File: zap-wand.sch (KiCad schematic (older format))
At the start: 15 parts, among them IC1 NC7WZ02, Q1 Q_PMOS_GDS, SW1 SW_PUSH_SMALL, U1 NCP4683DSQ33T1G

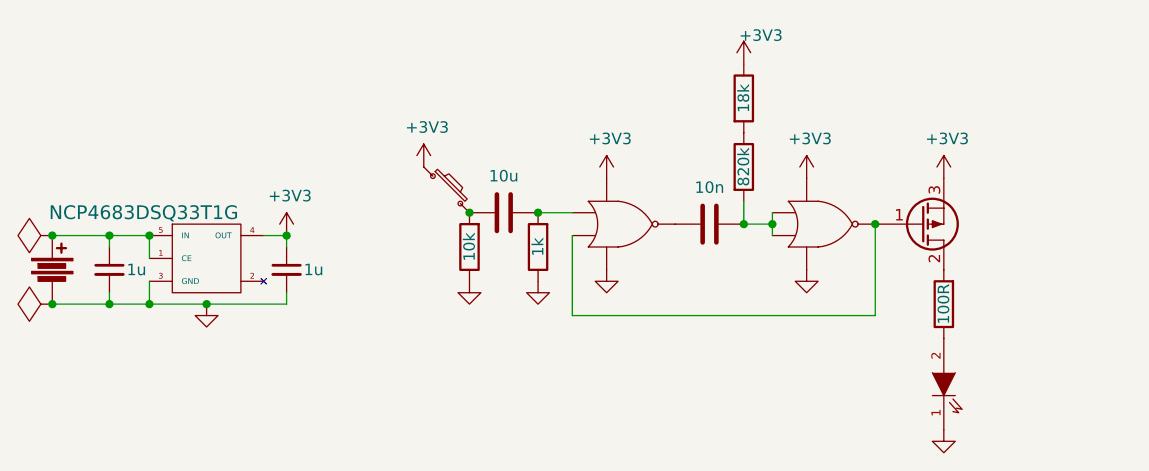
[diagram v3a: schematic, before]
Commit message: Added xor output inverter
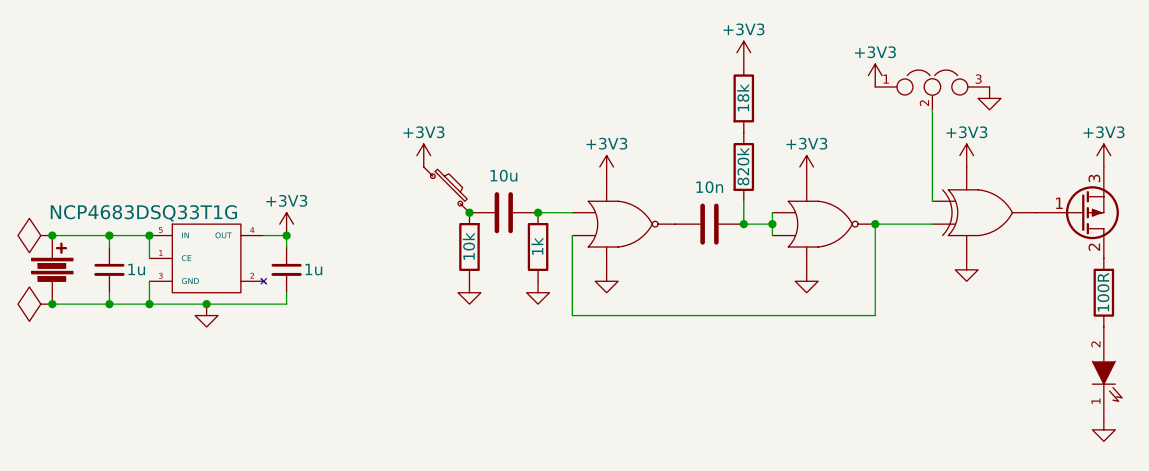
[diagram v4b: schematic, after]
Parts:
- added IC2: NC7SZ86, agg:SC-70-5, symbol NC7SZ86
- added JP1: JUMPER3, parts:solder_jumper_3, symbol JUMPER3
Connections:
- net +3V3: now also IC2.5 (VCC), JP1.1
- net GND: now also IC2.3 (GND), JP1.3
- net at IC1.2 (B1), IC1.3 (Y2): now also IC2.2 (B); no longer Q1.1 (G)
- new net: IC2.4 (Y), Q1.1 (G)
- new net: IC2.1 (A), JP1.2
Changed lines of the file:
@@
 LIBS:ncp103
 LIBS:ncp4683dsqxxt1g
+LIBS:nc7sz86
 LIBS:zap-wand-cache
 EELAYER 25 0
@@
 L LED D1
 U 1 1 578BAA6D
-P 5050 2550
-F 0 "D1" H 5096 2442 50  0001 R CNN
-F 1 "LED" V 5050 2442 50  0001 R CNN
-F 2 "agg:SIL-254P-02" H 5050 2550 50  0001 C CNN
-F 3 "" H 5050 2550 50  0000 C CNN
-	1    5050 2550
+P 5750 2500
+F 0 "D1" H 5796 2392 50  0001 R CNN
+F 1 "LED" V 5750 2392 50  0001 R CNN
+F 2 "agg:SIL-254P-02" H 5750 2500 50  0001 C CNN
+F 3 "" H 5750 2500 50  0000 C CNN
+	1    5750 2500
 	0    -1   -1   0
 $EndComp
@@
 L R R3
 U 1 1 578BAE5F
-P 5050 2200
-F 0 "R3" H 4980 2154 50  0001 R CNN
-F 1 "100R" V 5050 2200 50  0000 C CNN
-F 2 "agg:0603" V 4980 2200 50  0001 C CNN
-F 3 "http://www.farnell.com/datasheets/1849611.pdf?_ga=1.214886046.860814275.1465901405" H 5050 2200 50  0001 C CNN
-F 4 "2447227" H 5050 2200 60  0001 C CNN "Farnell"
-	1    5050 2200
+P 5750 2150
+F 0 "R3" H 5680 2104 50  0001 R CNN
+F 1 "100R" V 5750 2150 50  0000 C CNN
+F 2 "agg:0603" V 5680 2150 50  0001 C CNN
+F 3 "http://www.farnell.com/datasheets/1849611.pdf?_ga=1.214886046.860814275.1465901405" H 5750 2150 50  0001 C CNN
+F 4 "2447227" H 5750 2150 60  0001 C CNN "Farnell"
+	1    5750 2150
 	-1   0    0    1
 $EndComp
@@
 L Q_PMOS_GDS Q1
 U 1 1 578BD32A
-P 4950 1850
-F 0 "Q1" H 5141 1850 50  0001 L CNN
-F 1 "Q_PMOS_GDS" H 5141 1805 50  0001 L CNN
-F 2 "agg:SOT-323" H 5150 1950 50  0001 C CNN
-F 3 "http://www.farnell.com/datasheets/1508398.pdf?_ga=1.16462774.1253160071.1453215511" H 4950 1850 50  0001 C CNN
-F 4 "2069551" H 4950 1850 60  0001 C CNN "Farnell"
-	1    4950 1850
+P 5650 1800
+F 0 "Q1" H 5841 1800 50  0001 L CNN
+F 1 "Q_PMOS_GDS" H 5841 1755 50  0001 L CNN
+F 2 "agg:SOT-323" H 5850 1900 50  0001 C CNN
+F 3 "http://www.farnell.com/datasheets/1508398.pdf?_ga=1.16462774.1253160071.1453215511" H 5650 1800 50  0001 C CNN
+F 4 "2069551" H 5650 1800 60  0001 C CNN "Farnell"
+	1    5650 1800
 	1    0    0    1
 $EndComp
 $Comp
-L GND #PWR01
+L GND #PWR5
 U 1 1 578BBB69
 P 3275 2100
-F 0 "#PWR01" H 3275 1850 50  0001 C CNN
+F 0 "#PWR5" H 3275 1850 50  0001 C CNN
 F 1 "GND" H 3400 2025 50  0001 C CNN
 F 2 "" H 3275 2100 50  0000 C CNN
@@
 $EndComp
 $Comp
-L GND #PWR02
+L GND #PWR7
 U 1 1 578BBB54
 P 3575 2050
-F 0 "#PWR02" H 3575 1800 50  0001 C CNN
+F 0 "#PWR7" H 3575 1800 50  0001 C CNN
 F 1 "GND" H 3700 1975 50  0001 C CNN
 F 2 "" H 3575 2050 50  0000 C CNN
@@
 $EndComp
 $Comp
-L GND #PWR03
+L GND #PWR10
 U 1 1 578BBB38
 P 4450 2050
-F 0 "#PWR03" H 4450 1800 50  0001 C CNN
+F 0 "#PWR10" H 4450 1800 50  0001 C CNN
 F 1 "GND" H 4575 1975 50  0001 C CNN
 F 2 "" H 4450 2050 50  0000 C CNN
@@
 $EndComp
 $Comp
-L GND #PWR04
+L GND #PWR16
 U 1 1 578BBC2C
-P 5050 2750
-F 0 "#PWR04" H 5050 2500 50  0001 C CNN
-F 1 "GND" H 5175 2675 50  0001 C CNN
-F 2 "" H 5050 2750 50  0000 C CNN
-F 3 "" H 5050 2750 50  0000 C CNN
-	1    5050 2750
+P 5750 2700
+F 0 "#PWR16" H 5750 2450 50  0001 C CNN
+F 1 "GND" H 5875 2625 50  0001 C CNN
+F 2 "" H 5750 2700 50  0000 C CNN
+F 3 "" H 5750 2700 50  0000 C CNN
+	1    5750 2700
 	1    0    0    -1
 $EndComp
@@
 Connection ~ 4750 1850
 $Comp
-L GND #PWR05
+L GND #PWR1
 U 1 1 578BBB74
 P 1825 2200
-F 0 "#PWR05" H 1825 1950 50  0001 C CNN
+F 0 "#PWR1" H 1825 1950 50  0001 C CNN
 F 1 "GND" H 1950 2125 50  0001 C CNN
 F 2 "" H 1825 2200 50  0000 C CNN
@@
 $EndComp
 $Comp
-L +3V3 #PWR06
+L +3V3 #PWR2
 U 1 1 578CFCA7
 P 2175 1900
-F 0 "#PWR06" H 2175 1750 50  0001 C CNN
-F 1 "+3V3" H 2190 2073 50  0000 C CNN
+F 0 "#PWR2" H 2175 1750 50  0001 C CNN
+F 1 "+3V3" H 2175 2050 50  0000 C CNN
 F 2 "" H 2175 1900 50  0000 C CNN
 F 3 "" H 2175 1900 50  0000 C CNN
@@
 $EndComp
 $Comp
-L +3V3 #PWR07
+L +3V3 #PWR3
 U 1 1 578CFCC6
 P 2775 1600
-F 0 "#PWR07" H 2775 1450 50  0001 C CNN
-F 1 "+3V3" H 2790 1773 50  0000 C CNN
+F 0 "#PWR3" H 2775 1450 50  0001 C CNN
+F 1 "+3V3" H 2775 1750 50  0000 C CNN
 F 2 "" H 2775 1600 50  0000 C CNN
 F 3 "" H 2775 1600 50  0000 C CNN
@@
 $EndComp
 $Comp
-L +3V3 #PWR08
+L +3V3 #PWR6
 U 1 1 578CFCE3
 P 3575 1650
-F 0 "#PWR08" H 3575 1500 50  0001 C CNN
-F 1 "+3V3" H 3590 1823 50  0000 C CNN
+F 0 "#PWR6" H 3575 1500 50  0001 C CNN
+F 1 "+3V3" H 3575 1800 50  0000 C CNN
 F 2 "" H 3575 1650 50  0000 C CNN
 F 3 "" H 3575 1650 50  0000 C CNN
@@
 $EndComp
 $Comp
-L +3V3 #PWR09
+L +3V3 #PWR8
 U 1 1 578CFCF1
 P 4175 1150
-F 0 "#PWR09" H 4175 1000 50  0001 C CNN
-F 1 "+3V3" H 4250 1275 50  0000 C CNN
+F 0 "#PWR8" H 4175 1000 50  0001 C CNN
+F 1 "+3V3" H 4175 1300 50  0000 C CNN
 F 2 "" H 4175 1150 50  0000 C CNN
 F 3 "" H 4175 1150 50  0000 C CNN
@@
 $EndComp
 $Comp
-L +3V3 #PWR010
+L +3V3 #PWR9
 U 1 1 578CFCFF
 P 4450 1650
-F 0 "#PWR010" H 4450 1500 50  0001 C CNN
-F 1 "+3V3" H 4465 1823 50  0000 C CNN
+F 0 "#PWR9" H 4450 1500 50  0001 C CNN
+F 1 "+3V3" H 4450 1800 50  0000 C CNN
 F 2 "" H 4450 1650 50  0000 C CNN
 F 3 "" H 4450 1650 50  0000 C CNN
@@
 $EndComp
 $Comp
-L +3V3 #PWR011
+L +3V3 #PWR15
 U 1 1 578CFD0D
-P 5050 1650
-F 0 "#PWR011" H 5050 1500 50  0001 C CNN
-F 1 "+3V3" H 5065 1823 50  0000 C CNN
-F 2 "" H 5050 1650 50  0000 C CNN
-F 3 "" H 5050 1650 50  0000 C CNN
-	1    5050 1650
+P 5750 1600
+F 0 "#PWR15" H 5750 1450 50  0001 C CNN
+F 1 "+3V3" H 5750 1750 50  0000 C CNN
+F 2 "" H 5750 1600 50  0000 C CNN
+F 3 "" H 5750 1600 50  0000 C CNN
+	1    5750 1600
 	1    0    0    -1
 $EndComp
@@
 Connection ~ 2975 1800
 $Comp
-L GND #PWR012
+L GND #PWR4
 U 1 1 578E3BBA
 P 2975 2100
-F 0 "#PWR012" H 2975 1850 50  0001 C CNN
+F 0 "#PWR4" H 2975 1850 50  0001 C CNN
 F 1 "GND" H 3100 2025 50  0001 C CNN
 F 2 "" H 2975 2100 50  0000 C CNN
@@
 Connection ~ 1575 2200
 $Comp
-L PWR_FLAG #FLG013
+L PWR_FLAG #FLG1
 U 1 1 5790C912
 P 1150 1900
-F 0 "#FLG013" H 1150 1995 50  0001 C CNN
+F 0 "#FLG1" H 1150 1995 50  0001 C CNN
 F 1 "PWR_FLAG" V 1150 2078 50  0001 L CNN
 F 2 "" H 1150 1900 50  0000 C CNN
@@
 $EndComp
 $Comp
-L PWR_FLAG #FLG014
+L PWR_FLAG #FLG2
 U 1 1 5790C924
 P 1150 2200
-F 0 "#FLG014" H 1150 2295 50  0001 C CNN
+F 0 "#FLG2" H 1150 2295 50  0001 C CNN
 F 1 "PWR_FLAG" V 1150 2378 50  0001 L CNN
 F 2 "" H 1150 2200 50  0000 C CNN
@@
 Connection ~ 1150 1900
 Connection ~ 1150 2200
+$Comp
+L NC7SZ86 IC2
+U 1 1 57921ED8
+P 5250 1800
+F 0 "IC2" H 5491 1853 60  0001 L CNN
+F 1 "NC7SZ86" H 5491 1800 60  0001 L CNN
+F 2 "agg:SC-70-5" H 5250 1800 60  0001 C CNN
+F 3 "http://www.farnell.com/datasheets/680144.pdf?_ga=1.257304194.860814275.1465901405" H 5250 1800 60  0001 C CNN
+F 4 "1652016" H 5250 1800 60  0001 C CNN "Farnell"
+	1    5250 1800
+	1    0    0    -1
+$EndComp
+$Comp
+L +3V3 #PWR12
+U 1 1 57921F34
+P 5150 1600
+F 0 "#PWR12" H 5150 1450 50  0001 C CNN
+F 1 "+3V3" H 5150 1750 50  0000 C CNN
+F 2 "" H 5150 1600 50  0000 C CNN
+F 3 "" H 5150 1600 50  0000 C CNN
+	1    5150 1600
+	1    0    0    -1
+$EndComp
+$Comp
+L GND #PWR13
+U 1 1 57921F42
+P 5150 2000
+F 0 "#PWR13" H 5150 1750 50  0001 C CNN
+F 1 "GND" H 5275 1925 50  0001 C CNN
+F 2 "" H 5150 2000 50  0000 C CNN
+F 3 "" H 5150 2000 50  0000 C CNN
+	1    5150 2000
+	1    0    0    -1
+$EndComp
+Wire Wire Line
+	4750 1850 5000 1850
+$Comp
+L JUMPER3 JP1
+U 1 1 57922050
+P 5000 1250
+F 0 "JP1" H 5000 1398 50  0001 C CNN
+F 1 "JUMPER3" H 5000 1398 50  0001 C CNN
+F 2 "parts:solder_jumper_3" H 5000 1250 50  0001 C CNN
+F 3 "" H 5000 1250 50  0000 C CNN
+	1    5000 1250
+	1    0    0    -1
+$EndComp
+$Comp
+L +3V3 #PWR11
+U 1 1 579220A9
+P 4750 1250
+F 0 "#PWR11" H 4750 1100 50  0001 C CNN
+F 1 "+3V3" H 4750 1400 50  0000 C CNN
+F 2 "" H 4750 1250 50  0000 C CNN
+F 3 "" H 4750 1250 50  0000 C CNN
+	1    4750 1250
+	1    0    0    -1
+$EndComp
+$Comp
+L GND #PWR14
+U 1 1 57922131
+P 5250 1250
+F 0 "#PWR14" H 5250 1000 50  0001 C CNN
+F 1 "GND" H 5375 1175 50  0001 C CNN
+F 2 "" H 5250 1250 50  0000 C CNN
+F 3 "" H 5250 1250 50  0000 C CNN
+	1    5250 1250
+	1    0    0    -1
+$EndComp
+Wire Wire Line
+	5000 1750 5000 1350
 $EndSCHEMATC
